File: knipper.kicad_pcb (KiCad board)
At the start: 2 copper layers, 100 x 50 mm, 30 parts, among them J1 INPUT, J2 5V_REV_FROM_CONTROLLER, J3 REVLIGHTS, J4 DIR_RIGHT, J5 DIR_LEFT, Q1 IRF520N, Q2 IRF520N, Q3 IRF520N, SW5 DIRECTION_SWITCH, U1 NE555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

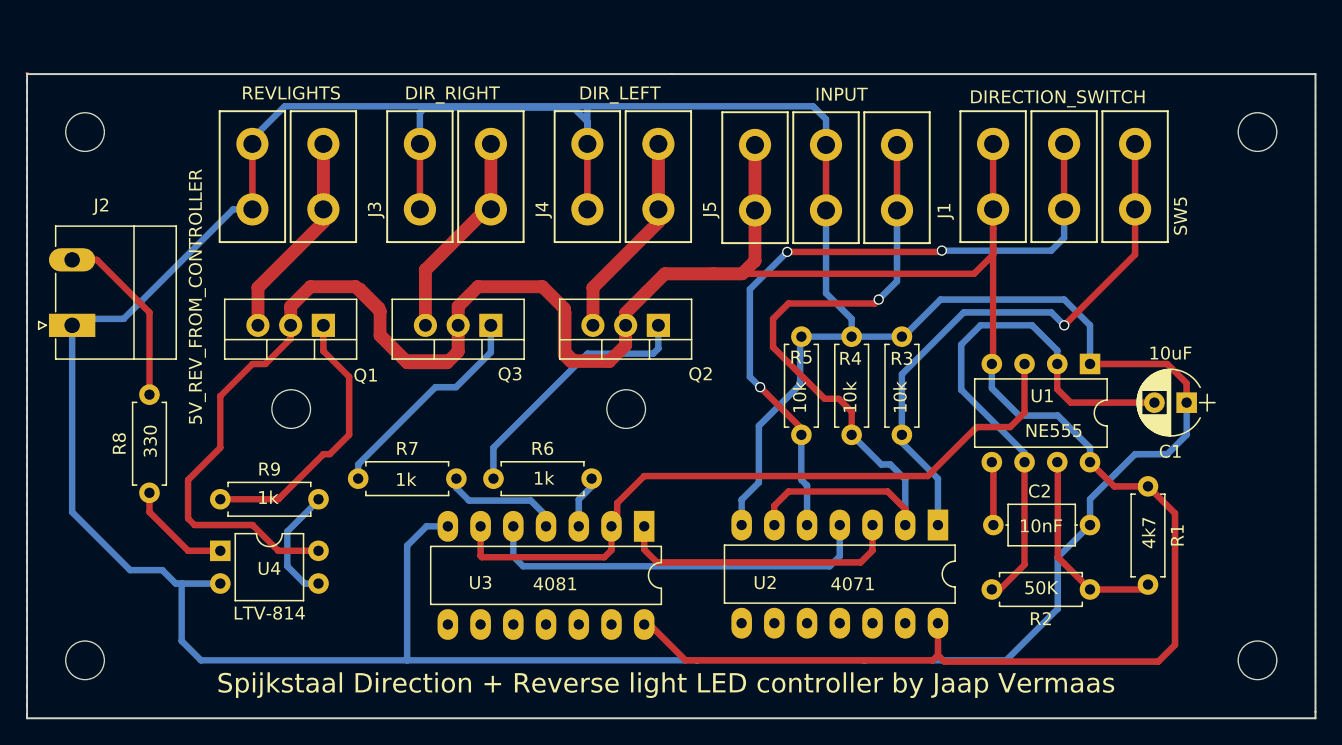
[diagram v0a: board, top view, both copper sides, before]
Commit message: implemented high side switching
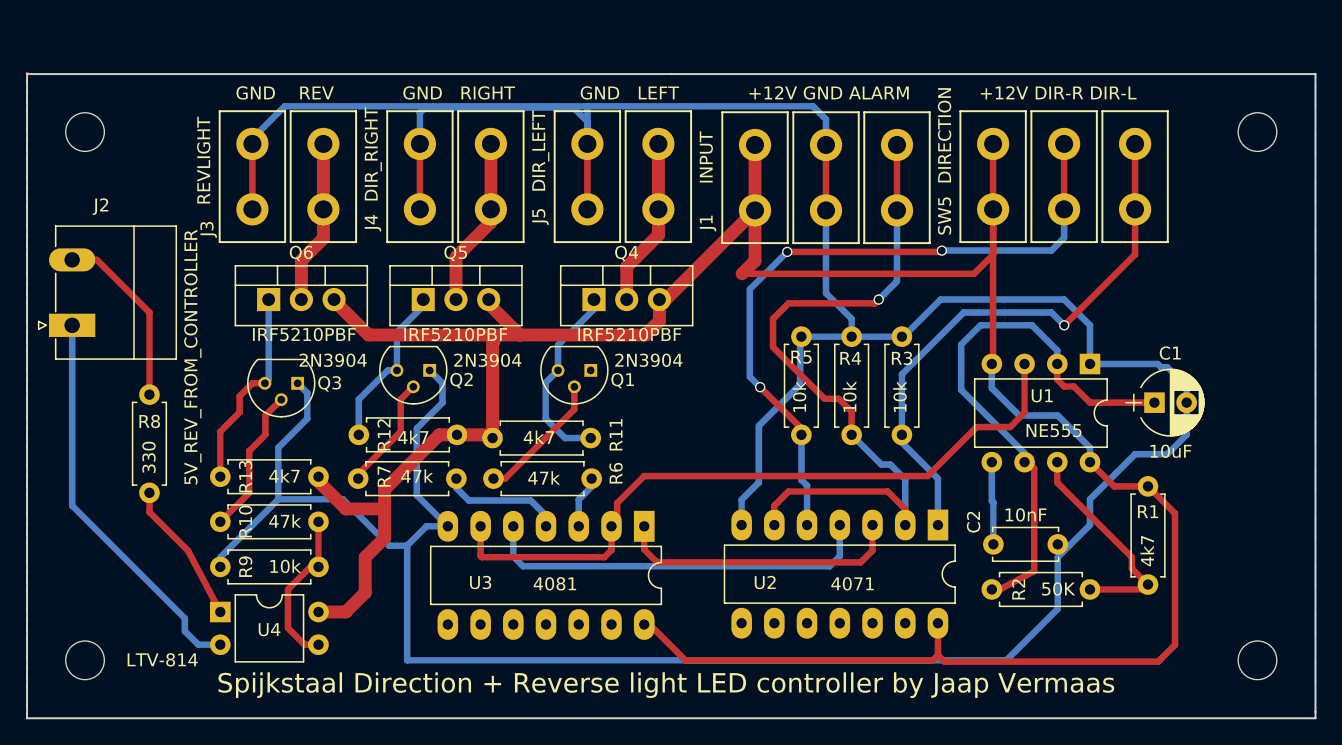
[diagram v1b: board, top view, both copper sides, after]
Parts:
- removed H5, H6: MOUNT_HOLE, knipper:MountingHole_3mm
- added Q4: IRF5210PBF, TO_SOT_Packages_THT:TO-220-3_Vertical, F.Cu at (94.0, 67.5)
- added Q5: IRF5210PBF, TO_SOT_Packages_THT:TO-220-3_Vertical, F.Cu at (80.8, 67.5)
- added Q6: IRF5210PBF, TO_SOT_Packages_THT:TO-220-3_Vertical, F.Cu at (68.8, 67.5)
- added R10: 47k, Resistors_THT:R_Axial_DIN0207_L6.3mm_D2.5mm_P7.62mm_Horizontal, F.Cu at (65.0, 84.8)
- added R11: 4k7, Resistors_THT:R_Axial_DIN0207_L6.3mm_D2.5mm_P7.62mm_Horizontal, F.Cu at (93.8, 78.2)
- added R12: 4k7, Resistors_THT:R_Axial_DIN0207_L6.3mm_D2.5mm_P7.62mm_Horizontal, F.Cu at (75.8, 78.0)
- added R13: 4k7, Resistors_THT:R_Axial_DIN0207_L6.3mm_D2.5mm_P7.62mm_Horizontal, F.Cu at (65.0, 81.2)
- C2: footprint Capacitors_THT:C_Axial_L5.1mm_D3.1mm_P7.50mm_Horizontal -> Capacitors_THT:C_Disc_D5.0mm_W2.5mm_P5.00mm
- J3: value REVLIGHTS -> REVLIGHT
- Q1, Q2, Q3: value IRF520N -> 2N3904; footprint TO_SOT_Packages_THT:TO-220_Vertical -> TO_SOT_Packages_THT:TO-92_Molded_Narrow
- R6, R7: value 1k -> 47k
- R9: value 1k -> 10k
- SW5: value DIRECTION_SWITCH -> DIRECTION
- moved Q1 21.0 mm to (93.8, 73.0)
- moved Q2 18.1 mm to (81.2, 73.0)
- moved Q3 15.7 mm to (71.0, 74.0)
- moved R9 5.25 mm to (65.0, 88.2)
- moved U4 4.75 mm to (65.0, 91.8)
- moved C1 2.50 mm to (137.5, 75.5), turned to 0 degrees
- moved C2 1.50 mm to (125.0, 86.5)
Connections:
- C1 pad 1: GND -> Net-(C1-Pad1)
- C1 pad 2: Net-(C1-Pad2) -> GND
- J2 pad 1: GND -> /E-GND
- Q1 pad 1: Net-(Q1-Pad1) -> GND
- Q1 pad 2: +12V -> Net-(Q1-Pad2)
- Q1 pad 3: Net-(J3-Pad1) -> Net-(Q1-Pad3)
- Q2 pad 1: Net-(Q2-Pad1) -> GND
- Q2 pad 2: +12V -> Net-(Q2-Pad2)
- Q2 pad 3: /DIR_L -> Net-(Q2-Pad3)
- Q3 pad 1: Net-(Q3-Pad1) -> GND
- Q3 pad 2: +12V -> Net-(Q3-Pad2)
- Q3 pad 3: /DIR_R -> Net-(Q3-Pad3)
- R2 pad 2: Net-(C1-Pad2) -> Net-(C1-Pad1)
- R6 pad 1: Net-(Q2-Pad1) -> Net-(Q1-Pad2)
- R7 pad 1: Net-(Q3-Pad1) -> Net-(Q2-Pad2)
- R9 pad 1: Net-(Q1-Pad1) -> GND
- U1 pad 2: Net-(C1-Pad2) -> Net-(C1-Pad1)
- U1 pad 6: Net-(C1-Pad2) -> Net-(C1-Pad1)
- U4 pad 2: GND -> /E-GND
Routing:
- net +12V: track 267.1 -> 214.9 mm
- net Net-(C1-Pad1): track 0.00 -> 43.1 mm
- net Net-(C1-Pad2): track 42.3 -> 0.00 mm
- net /E-GND: track 0.00 -> 31.3 mm
- net GND: track 308.8 -> 283.5 mm
- net Net-(Q1-Pad1): track 21.4 -> 0.00 mm
- net Net-(Q2-Pad1): track 20.2 -> 0.00 mm
- net Net-(Q3-Pad1): track 17.1 -> 0.00 mm
- net Net-(Q3-Pad3): track 0.00 -> 15.9 mm
- net Net-(Q1-Pad3): track 0.00 -> 14.9 mm
- net /DIR_R: track 27.5 -> 13.6 mm
- net Net-(Q2-Pad3): track 0.00 -> 13.0 mm
- net Net-(Q3-Pad2): track 0.00 -> 11.4 mm
- net Net-(Q1-Pad2): track 0.00 -> 10.3 mm
- net Net-(J3-Pad1): track 26.1 -> 16.5 mm
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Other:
- board text added: "+12V DIR-R DIR-L"
- board text added: "+12V GND ALARM"
- board text added: "GND LEFT"
- board text added: "GND REV"
- board text added: "GND RIGHT"

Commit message: Changed parts and layout to SMD
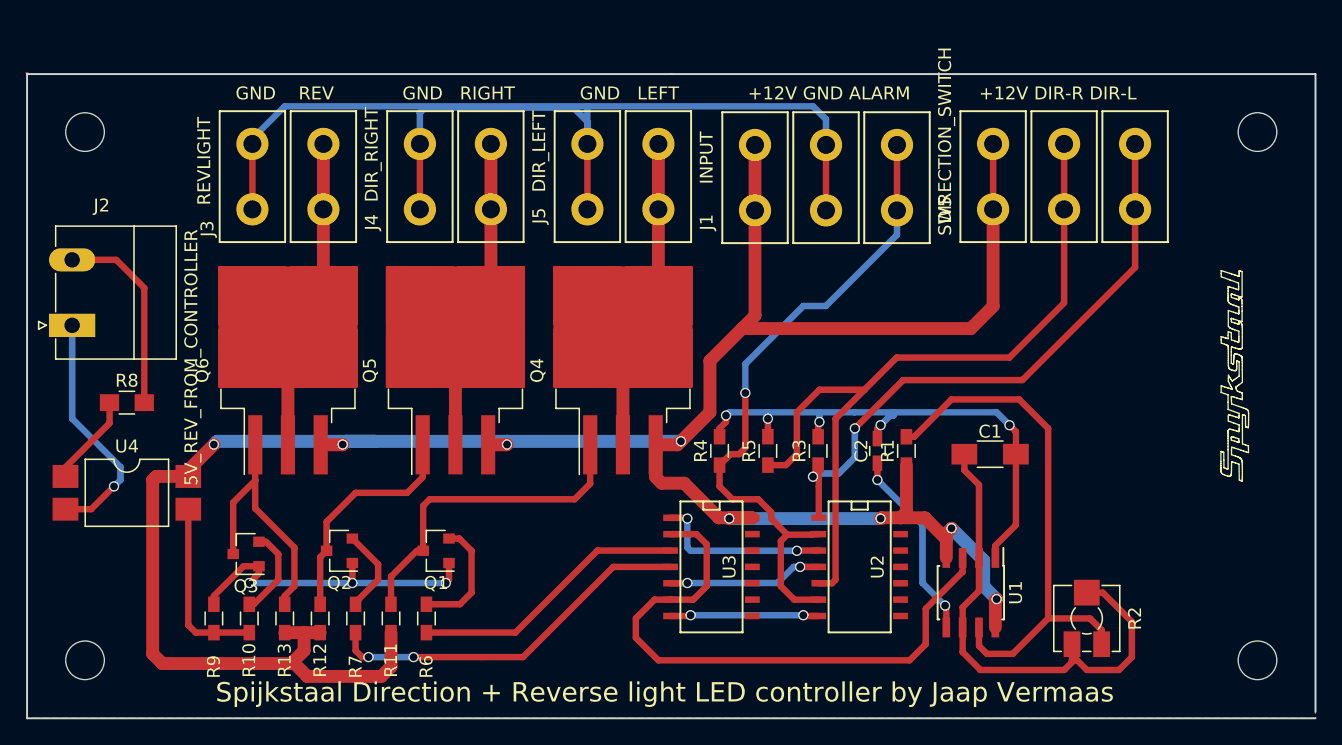
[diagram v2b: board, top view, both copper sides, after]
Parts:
- C1: footprint Capacitors_THT:CP_Radial_D5.0mm_P2.50mm -> Capacitors_SMD:C_1206_HandSoldering
- C2: footprint Capacitors_THT:C_Disc_D5.0mm_W2.5mm_P5.00mm -> Capacitors_SMD:C_0603_HandSoldering
- Q1, Q2, Q3: value 2N3904 -> BSR14; footprint TO_SOT_Packages_THT:TO-92_Molded_Narrow -> TO_SOT_Packages_SMD:SOT-23
- Q4, Q5, Q6: value IRF5210PBF -> IRF5210STRLPBF; footprint TO_SOT_Packages_THT:TO-220-3_Vertical -> TO_SOT_Packages_SMD:TO-263-3_TabPin2
- R1, R10, R11, R12, R13, R3, R4, R5, R6, R7, R9: footprint Resistors_THT:R_Axial_DIN0207_L6.3mm_D2.5mm_P7.62mm_Horizontal -> Resistors_SMD:R_0603_HandSoldering
- R2: value 50K -> 100K; footprint Resistors_THT:R_Axial_DIN0207_L6.3mm_D2.5mm_P7.62mm_Horizontal -> Potentiometers:Potentiometer_Trimmer_Vishay_TS53YJ
- R8: footprint Resistors_THT:R_Axial_DIN0207_L6.3mm_D2.5mm_P7.62mm_Horizontal -> Resistors_SMD:R_0805_HandSoldering
- SW5: value DIRECTION -> DIRECTION_SWITCH
- U1: value NE555 -> NE555D; footprint Housings_DIP:DIP-8_W7.62mm -> Housings_SOIC:SOIC-8_3.9x4.9mm_Pitch1.27mm
- U2: value 4071 -> CD4071BM; footprint Housings_DIP:DIP-14_W7.62mm_LongPads -> SMD_Packages:SOIC-14_N
- U3: value 4081 -> CD4081BM; footprint Housings_DIP:DIP-14_W7.62mm_LongPads -> SMD_Packages:SOIC-14_N
- U4: value LTV-814 -> FOD814SD; footprint Housings_DIP:DIP-4_W7.62mm -> Housings_DIP:SMDIP-4_W9.53mm
- moved R11 20.9 mm to (78.2, 92.2), turned to 270 degrees
- moved U1 20.0 mm to (123.2, 90.2)
- moved R1 19.0 mm to (118.2, 79.2), turned to 90 degrees
- moved Q1 18.4 mm to (81.8, 87.0)
- moved Q2 15.7 mm to (74.2, 87.0)
- moved R12 14.6 mm to (72.8, 92.2), turned to 270 degrees
- moved Q3 13.8 mm to (67.0, 87.2)
- moved C1 13.4 mm to (124.8, 79.5)
- moved R13 12.1 mm to (70.0, 92.2), turned to 270 degrees
- moved R6 12.0 mm to (81.0, 92.2), turned to 270 degrees
- moved U4 11.8 mm to (57.8, 82.5)
- moved C2 11.6 mm to (116.0, 79.2), turned to 90 degrees
- moved R7 10.9 mm to (75.5, 92.2), turned to 270 degrees
- moved R4 10.3 mm to (103.8, 79.2)
- moved R10 7.83 mm to (67.2, 92.2), turned to 270 degrees
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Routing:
- net GND: track 283.5 -> 169.1 mm, vias 0 -> 10
- net Net-(R1-Pad2): track 17.1 -> 41.7 mm
- net Net-(R7-Pad2): track 9.39 -> 29.0 mm, vias 0 -> 2
- net Net-(U2-Pad4): track 30.7 -> 12.0 mm, vias 0 -> 2
- net +12V: track 214.9 -> 196.6 mm, vias 0 -> 8
- net Net-(R6-Pad2): track 4.11 -> 21.6 mm
- net /DIR_R: track 13.6 -> 25.9 mm
- net /E-GND: track 31.3 -> 19.5 mm, vias 0 -> 1
- net /DIR_L: track 15.1 -> 26.5 mm
- net Net-(J3-Pad1): track 16.5 -> 27.3 mm
- net Net-(Q1-Pad3): track 14.9 -> 25.7 mm
- net Net-(U1-Pad3): track 54.9 -> 46.0 mm
- net Net-(U2-Pad3): track 22.3 -> 13.9 mm, vias 0 -> 2
- net Net-(C2-Pad1): track 6.60 -> 15.0 mm, vias 0 -> 2
- net /RIGHT: track 53.5 -> 59.5 mm, vias 3 -> 0
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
